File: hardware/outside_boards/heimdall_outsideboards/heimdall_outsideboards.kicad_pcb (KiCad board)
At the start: 2 copper layers, 1 part, among them IC1 CLRC66303HNY

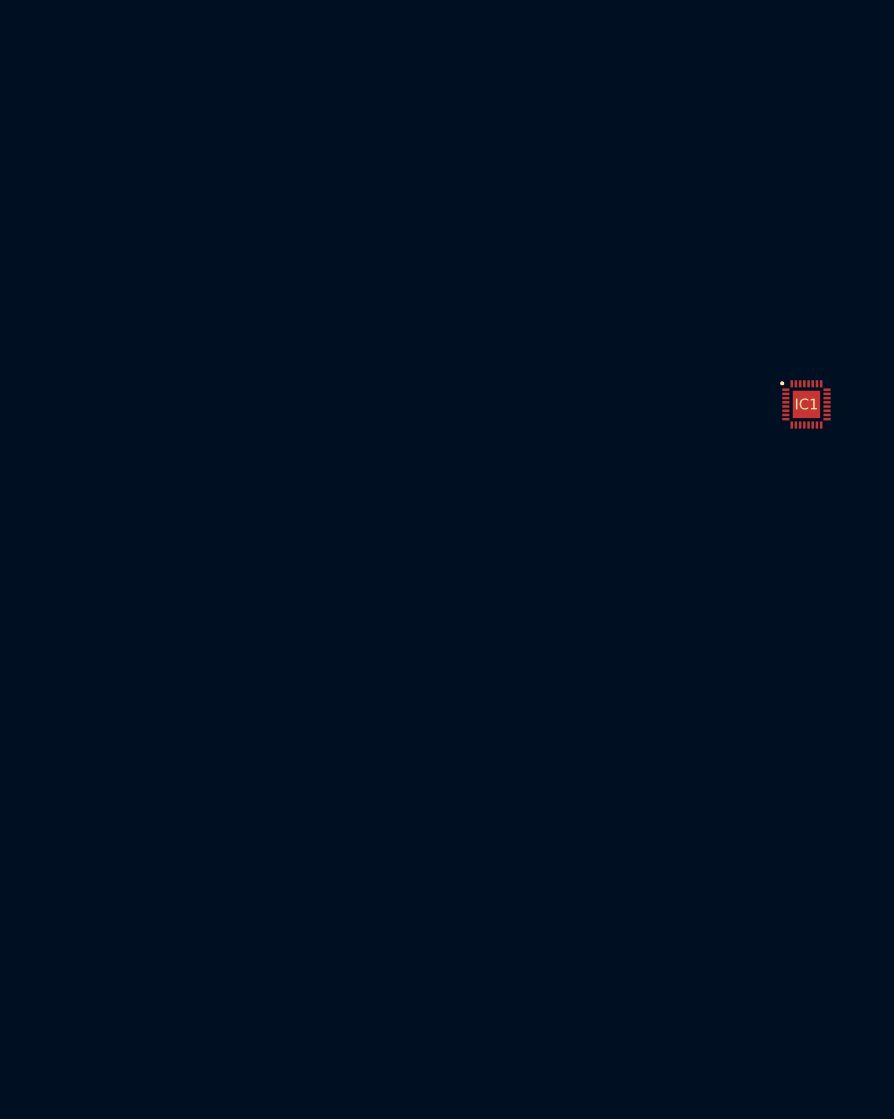
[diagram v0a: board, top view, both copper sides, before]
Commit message: Finished adding footprints
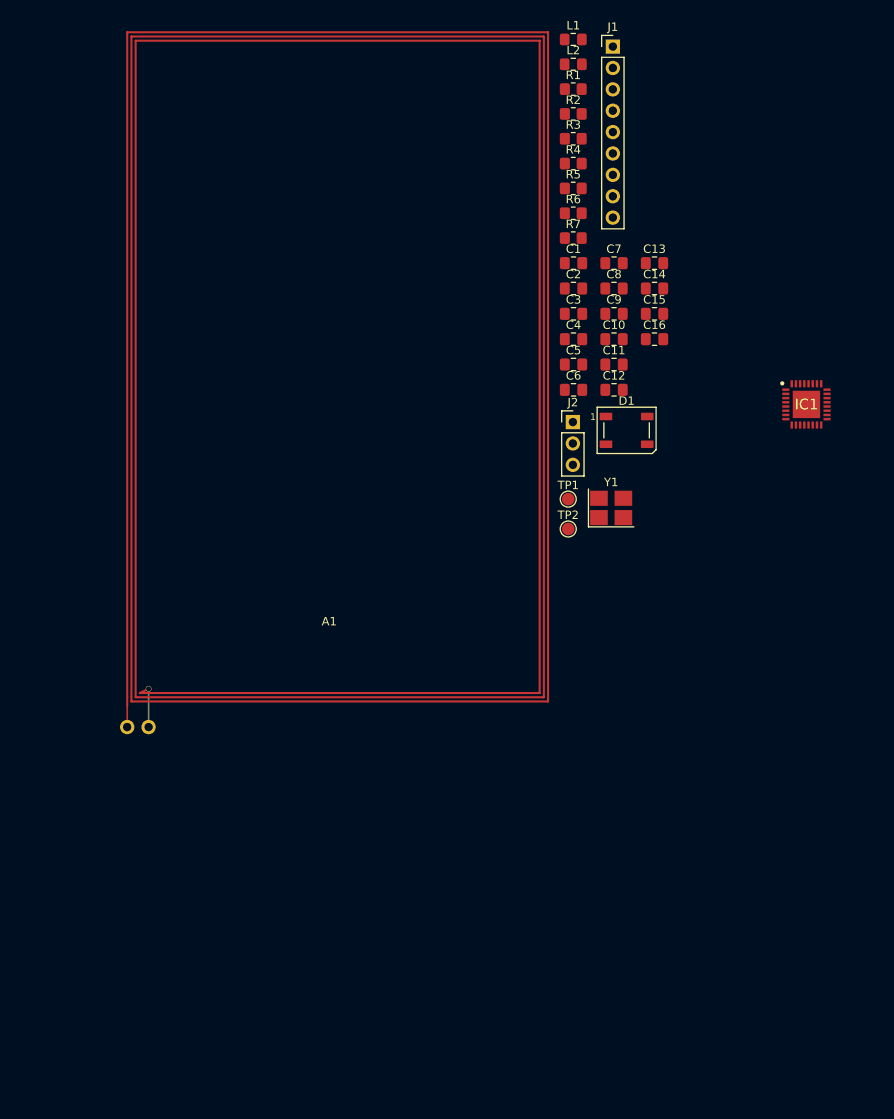
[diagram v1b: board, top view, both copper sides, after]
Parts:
- added A1: ~, Heimdall:Anetnna_50x80, F.Cu at (57.1, 109.3)
- added C1: 122.2pf, Capacitor_SMD:C_0805_2012Metric_Pad1.18x1.45mm_HandSolder, F.Cu at (110.1, 56.8)
- added C10: 10pf, Capacitor_SMD:C_0805_2012Metric_Pad1.18x1.45mm_HandSolder, F.Cu at (114.9, 65.8)
- added C11: 100nF, Capacitor_SMD:C_0805_2012Metric_Pad1.18x1.45mm_HandSolder, F.Cu at (114.9, 68.8)
- added C12: 1uF, Capacitor_SMD:C_0805_2012Metric_Pad1.18x1.45mm_HandSolder, F.Cu at (114.9, 71.8)
- added C13: 100nF, Capacitor_SMD:C_0805_2012Metric_Pad1.18x1.45mm_HandSolder, F.Cu at (119.7, 56.8)
- added C14: 10pf, Capacitor_SMD:C_0805_2012Metric_Pad1.18x1.45mm_HandSolder, F.Cu at (119.7, 59.8)
- added C15: 1nF, Capacitor_SMD:C_0805_2012Metric_Pad1.18x1.45mm_HandSolder, F.Cu at (119.7, 62.8)
- added C16: 1nF, Capacitor_SMD:C_0805_2012Metric_Pad1.18x1.45mm_HandSolder, F.Cu at (119.7, 65.8)
- added C2: 122.2pf, Capacitor_SMD:C_0805_2012Metric_Pad1.18x1.45mm_HandSolder, F.Cu at (110.1, 59.8)
- added C3: 34.7pf, Capacitor_SMD:C_0805_2012Metric_Pad1.18x1.45mm_HandSolder, F.Cu at (110.1, 62.8)
- added C4: 34.7pf, Capacitor_SMD:C_0805_2012Metric_Pad1.18x1.45mm_HandSolder, F.Cu at (110.1, 65.8)
- added C5: 108.7pf, Capacitor_SMD:C_0805_2012Metric_Pad1.18x1.45mm_HandSolder, F.Cu at (110.1, 68.8)
- added C6: 108.7pf, Capacitor_SMD:C_0805_2012Metric_Pad1.18x1.45mm_HandSolder, F.Cu at (110.1, 71.8)
- added C7: 2.1pf, Capacitor_SMD:C_0805_2012Metric_Pad1.18x1.45mm_HandSolder, F.Cu at (114.9, 56.8)
- added C8: 470nF, Capacitor_SMD:C_0805_2012Metric_Pad1.18x1.45mm_HandSolder, F.Cu at (114.9, 59.8)
- added C9: 470nF, Capacitor_SMD:C_0805_2012Metric_Pad1.18x1.45mm_HandSolder, F.Cu at (114.9, 62.8)
- added D1: WS2812B, LED_SMD:LED_WS2812B_PLCC4_5.0x5.0mm_P3.2mm, F.Cu at (116.4, 76.6)
- added J1: Motherboard, Connector_PinHeader_2.54mm:PinHeader_1x09_P2.54mm_Vertical, F.Cu at (114.8, 31.0)
- added J2: LED Out, Connector_PinHeader_2.54mm:PinHeader_1x03_P2.54mm_Vertical, F.Cu at (110.0, 75.7)
- added L1: 470nH, Inductor_SMD:L_0805_2012Metric_Pad1.15x1.40mm_HandSolder, F.Cu at (110.0, 30.2)
- added L2: 470nH, Inductor_SMD:L_0805_2012Metric_Pad1.15x1.40mm_HandSolder, F.Cu at (110.0, 33.1)
- added R1: 1.03, Resistor_SMD:R_0805_2012Metric_Pad1.20x1.40mm_HandSolder, F.Cu at (110.0, 36.1)
- added R2: 1.03, Resistor_SMD:R_0805_2012Metric_Pad1.20x1.40mm_HandSolder, F.Cu at (110.0, 39.0)
- added R3: 2.224, Resistor_SMD:R_0805_2012Metric_Pad1.20x1.40mm_HandSolder, F.Cu at (110.0, 42.0)
- added R4: 1k, Resistor_SMD:R_0805_2012Metric_Pad1.20x1.40mm_HandSolder, F.Cu at (110.0, 44.9)
- added R5: 12k, Resistor_SMD:R_0805_2012Metric_Pad1.20x1.40mm_HandSolder, F.Cu at (110.0, 47.9)
- added R6: 1k, Resistor_SMD:R_0805_2012Metric_Pad1.20x1.40mm_HandSolder, F.Cu at (110.0, 50.8)
- added R7: 12k, Resistor_SMD:R_0805_2012Metric_Pad1.20x1.40mm_HandSolder, F.Cu at (110.0, 53.8)
- added TP1: TestPoint, TestPoint:TestPoint_Pad_D1.5mm, F.Cu at (109.5, 84.8)
- added TP2: TestPoint, TestPoint:TestPoint_Pad_D1.5mm, F.Cu at (109.5, 88.3)
- added Y1: 27.12MHz, Crystal:Crystal_SMD_3225-4Pin_3.2x2.5mm_HandSoldering, F.Cu at (114.5, 85.8)
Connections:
- IC1 pad 12: unconnected-(IC1-RXP-Pad12) -> Net-(IC1-RXP)
- IC1 pad 13: unconnected-(IC1-RXN-Pad13) -> Net-(IC1-RXN)
- IC1 pad 14: unconnected-(IC1-VMID-Pad14) -> Net-(IC1-VMID)
- IC1 pad 15: unconnected-(IC1-TX2-Pad15) -> Net-(IC1-TX2)
- IC1 pad 16: unconnected-(IC1-TVSS-Pad16) -> GND
- IC1 pad 17: unconnected-(IC1-TX1-Pad17) -> Net-(IC1-TX1)
- IC1 pad 18: unconnected-(IC1-TVDD-Pad18) -> +5V
- IC1 pad 19: unconnected-(IC1-XTAL1-Pad19) -> XTAL1
- IC1 pad 20: unconnected-(IC1-XTAL2-Pad20) -> XTAL2
- IC1 pad 25: unconnected-(IC1-PVDD-Pad25) -> +3.3V
- IC1 pad 26: unconnected-(IC1-IFSEL0/OUT4-Pad26) -> GND
- IC1 pad 27: unconnected-(IC1-IFSEL1/OUT5-Pad27) -> +3.3V
- IC1 pad 28: unconnected-(IC1-IF0-Pad28) -> MOSI
- IC1 pad 29: unconnected-(IC1-IF1-Pad29) -> SCK
- IC1 pad 30: unconnected-(IC1-IF2-Pad30) -> MISO
- IC1 pad 31: unconnected-(IC1-IF3-Pad31) -> CS
- IC1 pad 33: unconnected-(IC1-VSS-Pad33) -> GND
- IC1 pad 7: unconnected-(IC1-DVDD-Pad7) -> Net-(IC1-DVDD)
- IC1 pad 8: unconnected-(IC1-VDD-Pad8) -> +3.3V
- IC1 pad 9: unconnected-(IC1-AVDD-Pad9) -> Net-(IC1-AVDD)

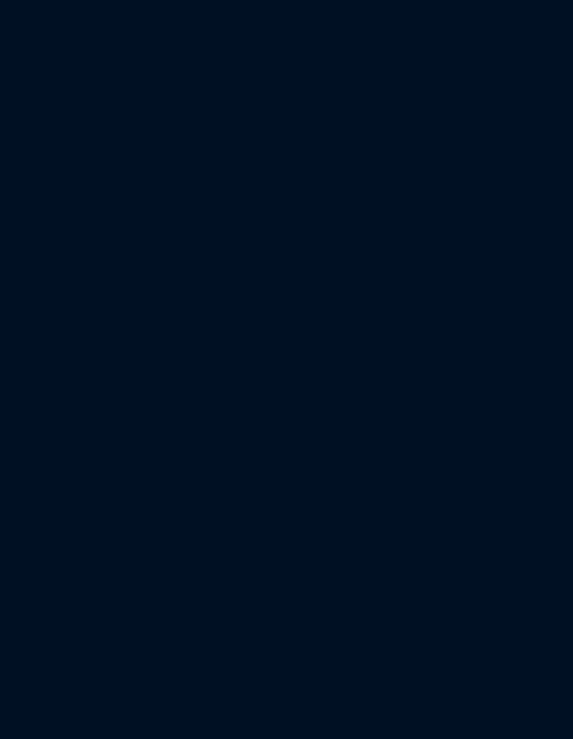
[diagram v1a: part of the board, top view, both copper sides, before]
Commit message: Added a buzzer
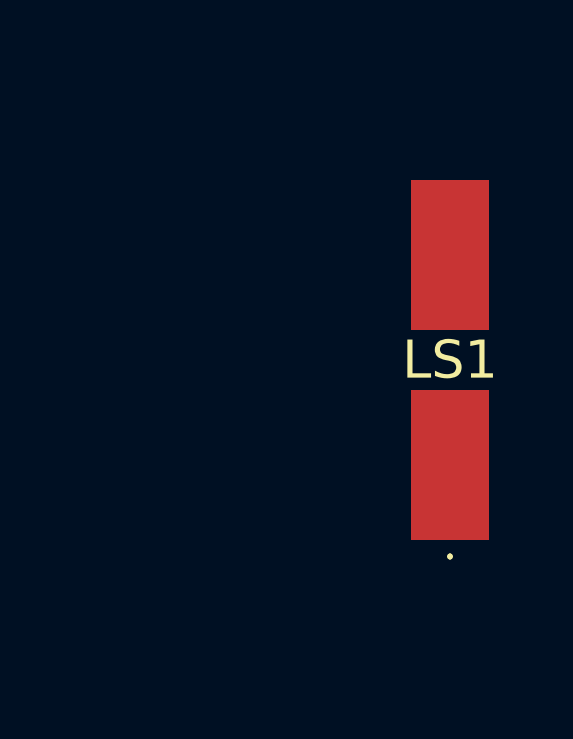
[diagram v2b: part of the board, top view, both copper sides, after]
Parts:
- added LS1: CMT-1075-SMT-TR, CLRC663:CMT1075SMTTR, F.Cu at (144.0, 97.0)

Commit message: Working on PCB layout
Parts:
- moved J1 131.7 mm to (63.5, 152.4), turned to 90 degrees
- moved L1 115.4 mm to (59.4, 133.9), turned to 90 degrees
- moved L2 114.2 mm to (56.1, 133.9), turned to 90 degrees
- moved R1 104.0 mm to (56.1, 125.0), turned to 90 degrees
- moved R5 102.9 mm to (52.1, 132.8)
- moved R4 101.6 mm to (78.5, 141.5), turned to 90 degrees
- moved C15 100.1 mm to (48.3, 132.8)
- moved R2 99.7 mm to (59.4, 125.0), turned to 90 degrees
- moved J2 96.9 mm to (50.8, 152.4), turned to 90 degrees
- moved R6 95.3 mm to (80.5, 141.5), turned to -90 degrees
- moved C1 93.8 mm to (51.8, 130.3), turned to 180 degrees
- moved D1 92.5 mm to (53.4, 144.4)
- moved R3 92.2 mm to (56.1, 116.8), turned to 90 degrees
- moved R7 91.6 mm to (63.8, 132.8), turned to 180 degrees
- moved C8 88.2 mm to (71.5, 136.5)
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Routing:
- net +5V: track 0.00 -> 25.3 mm
- net Beeper: track 0.00 -> 10.7 mm
- net GND: track 0.00 -> 7.64 mm, vias 0 -> 16
- net LED Out: track 0.00 -> 7.33 mm
- net Net-(IC1-DVDD): track 0.00 -> 3.33 mm
- net Net-(IC1-AVDD): track 0.00 -> 2.94 mm
- net Net-(A1-Pad2): track 0.00 -> 2.68 mm
- net Net-(A1-Pad1): track 0.00 -> 2.16 mm
- added copper zone on F.Cu, net +3.3V
- added copper zone on B.Cu, net GND
